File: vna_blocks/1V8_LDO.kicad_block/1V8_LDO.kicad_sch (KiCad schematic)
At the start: 8 parts, among them U36 LT3041ADE-PBF

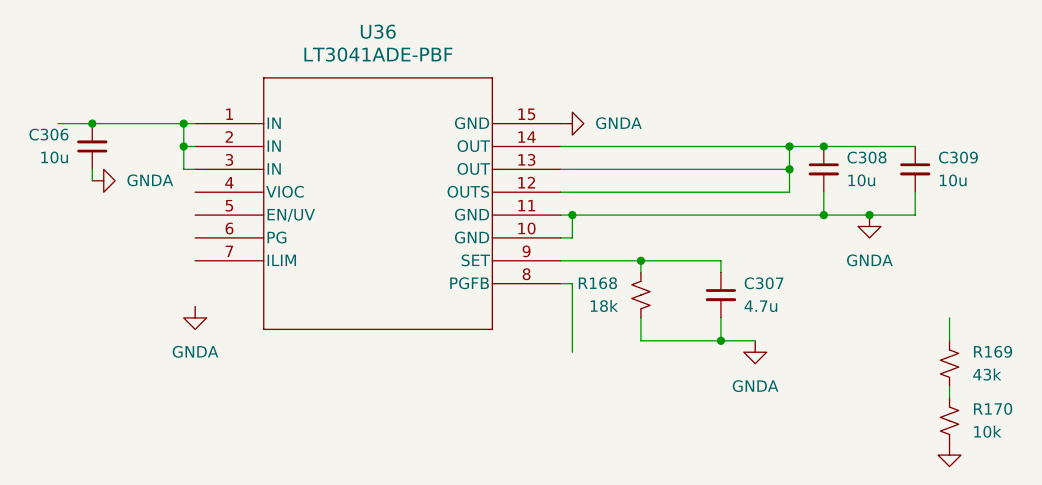
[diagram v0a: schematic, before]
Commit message: fixed IC courtyard issues
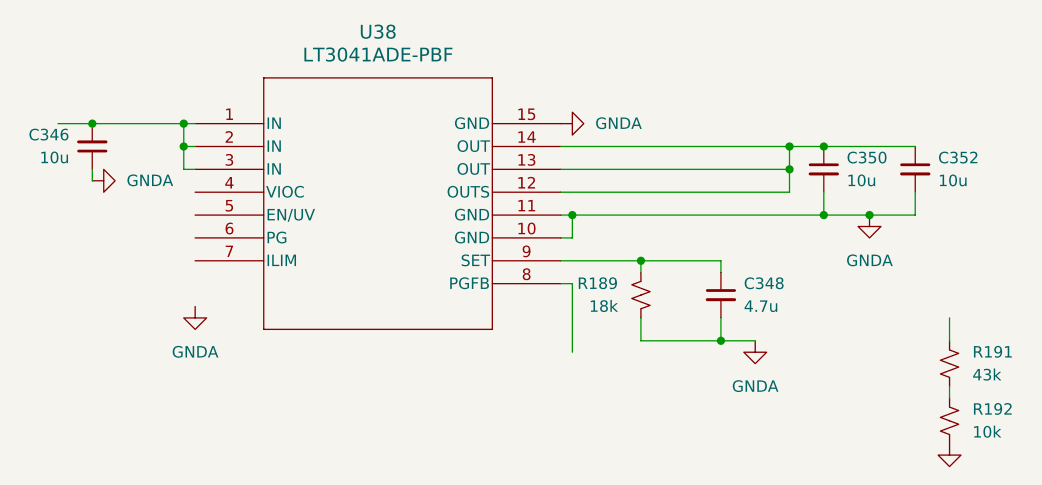
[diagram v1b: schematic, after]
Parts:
- renumbered C306 to C346, C307 to C348, C308 to C350, C309 to C352, R168 to R189, R169 to R191, R170 to R192, U36 to U38
